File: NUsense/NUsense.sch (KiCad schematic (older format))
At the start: 0 parts

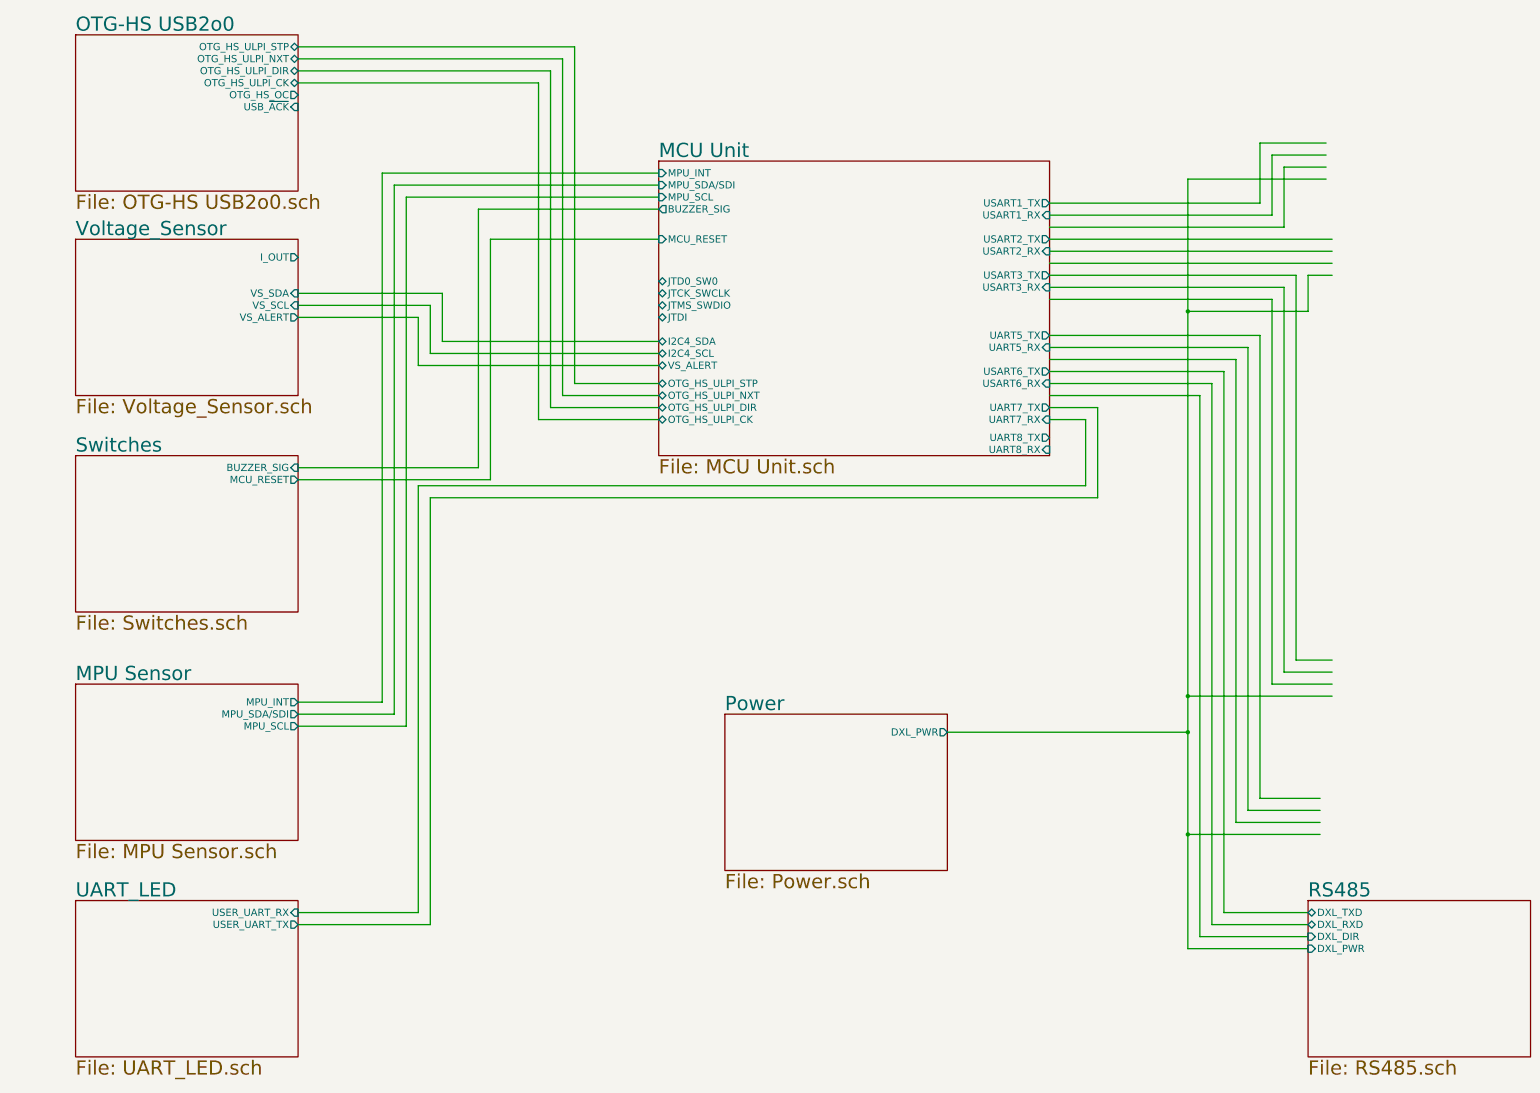
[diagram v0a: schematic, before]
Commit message: Adds all 5 RS485 sheets
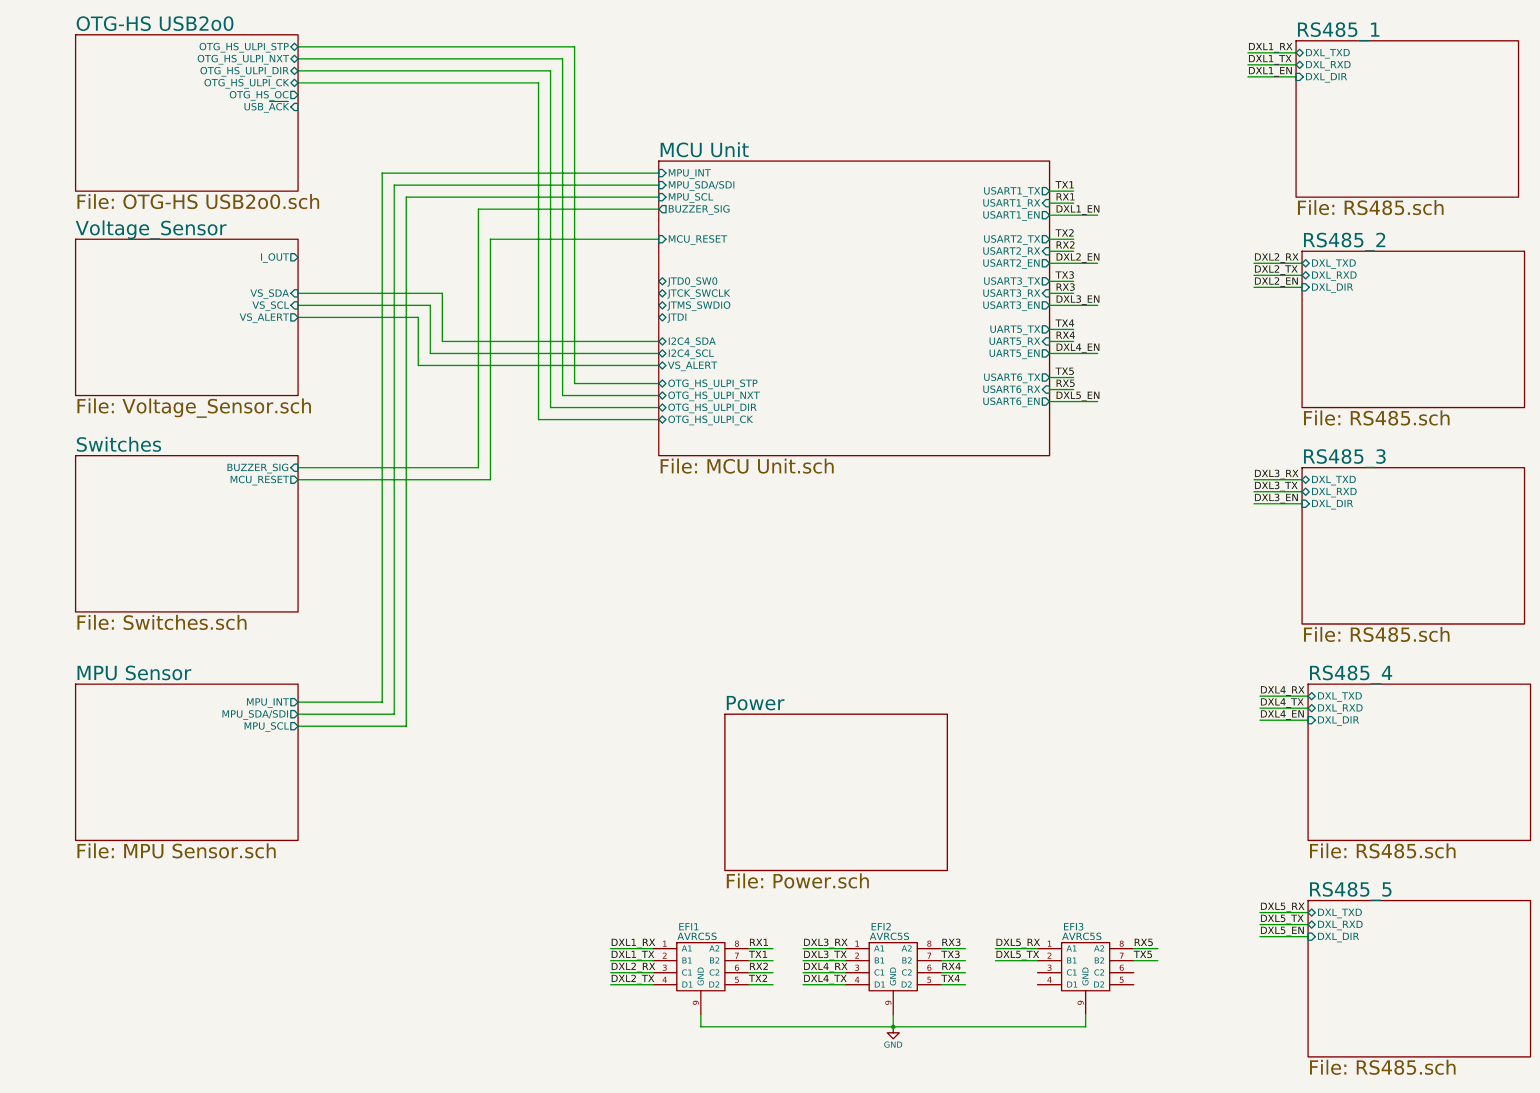
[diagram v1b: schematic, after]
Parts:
- added EFI1, EFI2, EFI3: AVRC5S, Footprints:0805_NET_4, symbol AVRC5S
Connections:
- net labels added: DXL1_EN, DXL1_RX, DXL1_TX, DXL2_EN, DXL2_RX, DXL2_TX, DXL3_EN, DXL3_RX, DXL3_TX, DXL4_EN, DXL4_RX, DXL4_TX, DXL5_EN, DXL5_RX, DXL5_TX, GND, RX1, RX2, RX3, RX4, RX5, TX1, TX2, TX3, TX4, TX5
- wire segments 94 -> 90

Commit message: More Changes
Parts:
- renumbered EFI1 to EFI101, EFI2 to EFI102, EFI3 to EFI103
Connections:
- net labels added: BATT_+, BATT_-, DXL_PWR_EN
- wire segments 90 -> 96
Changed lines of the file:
@@
 F31 "UART5_EN" O R 10450 3800 60
 F32 "USART3_EN" O R 10450 3400 60
+F33 "DXL_PWR_EN" O R 10450 4400 60
 $EndSheet
 $Sheet
@@
 F4 "VS_SDA" I R 4200 3300 60
 F5 "VS_ALERT" O R 4200 3500 60
+F6 "BATT_+" B R 4200 3750 60
+F7 "BATT_-" B R 4200 3850 60
 $EndSheet
 Wire Wire Line
@@
 	4900 2300 7200 2300
 $Comp
-L AVRC5S EFI2
+L AVRC5S EFI102
 U 1 1 5A73E86C
 P 8950 9100
-F 0 "EFI2" H 9050 9630 60  0000 C CNN
+F 0 "EFI102" H 9050 9630 60  0000 C CNN
 F 1 "AVRC5S" H 9120 9550 60  0000 C CNN
 F 2 "Footprints:0805_NET_4" H 9100 9150 60  0001 C CNN
@@
 $EndComp
 $Comp
-L AVRC5S EFI3
+L AVRC5S EFI103
 U 1 1 5A73EA25
 P 10550 9100
-F 0 "EFI3" H 10650 9630 60  0000 C CNN
+F 0 "EFI103" H 10650 9630 60  0000 C CNN
 F 1 "AVRC5S" H 10720 9550 60  0000 C CNN
 F 2 "Footprints:0805_NET_4" H 10700 9150 60  0001 C CNN
@@
 $EndComp
 $Comp
-L AVRC5S EFI1
+L AVRC5S EFI101
 U 1 1 5A73EB9C
 P 7350 9100
-F 0 "EFI1" H 7450 9630 60  0000 C CNN
+F 0 "EFI101" H 7450 9630 60  0000 C CNN
 F 1 "AVRC5S" H 7520 9550 60  0000 C CNN
 F 2 "Footprints:0805_NET_4" H 7500 9150 60  0001 C CNN
@@
 Connection ~ 9150 9400
 $Comp
-L GND #PWR?
+L GND #PWR01
 U 1 1 5A7404A8
 P 9150 9400
-F 0 "#PWR?" H 9150 9150 50  0001 C CNN
+F 0 "#PWR01" H 9150 9150 50  0001 C CNN
 F 1 "GND" H 9150 9250 50  0000 C CNN
 F 2 "" H 9150 9400 50  0001 C CNN
@@
 F0 "Power" 118
 F1 "Power.sch" 118
+F2 "DXL_PWR_EN" I R 9600 6950 60
+F3 "BATT_+" B R 9600 7200 60
+F4 "BATT_-" B R 9600 7300 60
 $EndSheet
 Wire Wire Line
@@
 Wire Wire Line
 	10450 4200 10850 4200
+Wire Wire Line
+	10450 4400 11050 4400
+Text Label 11050 4400 2    60   ~ 0
+DXL_PWR_EN
+Wire Wire Line
+	9600 6950 10300 6950
+Text Label 10300 6950 2    60   ~ 0
+DXL_PWR_EN
+Wire Wire Line
+	4200 3750 4650 3750
+Wire Wire Line
+	4200 3850 4650 3850
+Wire Wire Line
+	9600 7200 10250 7200
+Wire Wire Line
+	9600 7300 10250 7300
+Text Label 10250 7200 2    60   ~ 0
+BATT_+
+Text Label 10250 7300 2    60   ~ 0
+BATT_-
+Text Label 4650 3850 2    60   ~ 0
+BATT_-
+Text Label 4650 3750 2    60   ~ 0
+BATT_+
 $EndSCHEMATC

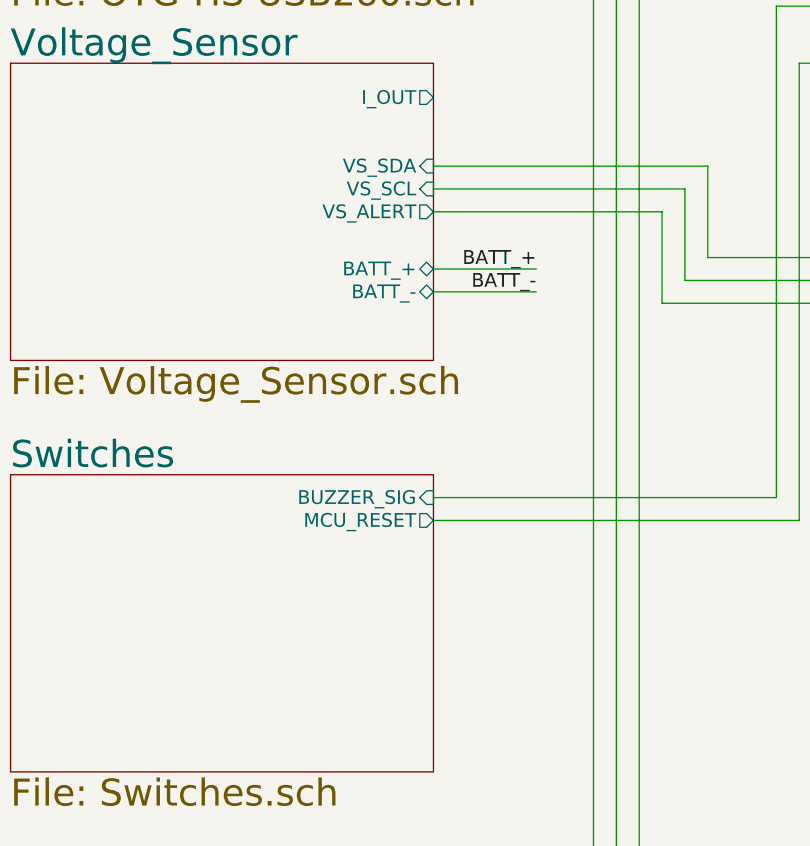
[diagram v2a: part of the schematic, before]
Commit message: Fan PWM
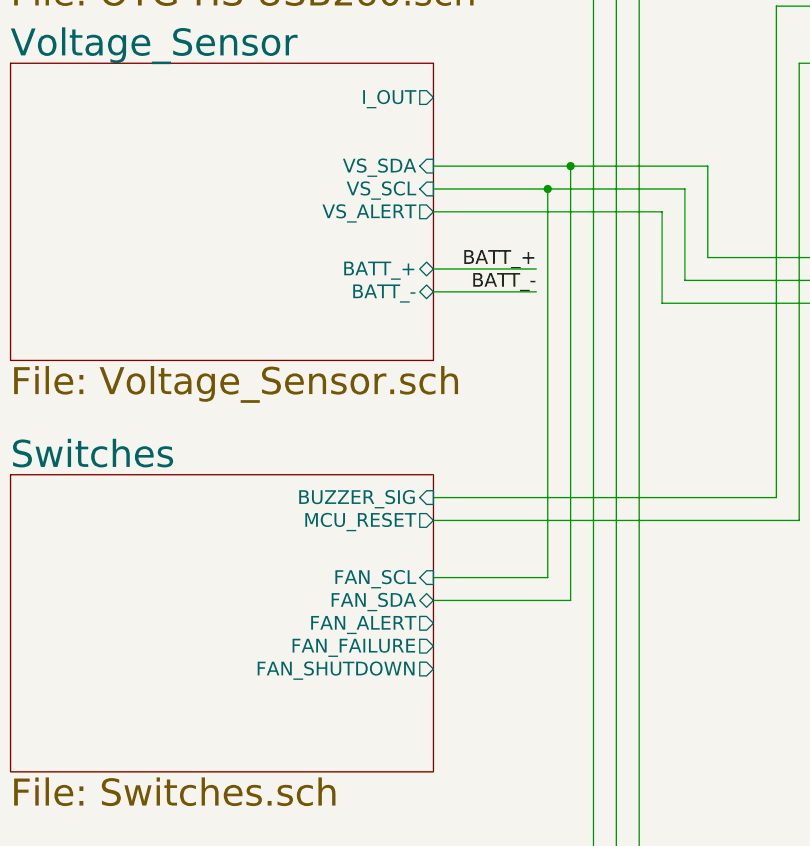
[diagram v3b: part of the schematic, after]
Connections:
- wire segments 96 -> 100
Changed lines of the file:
@@
 F2 "BUZZER_SIG" I R 4200 4750 60
 F3 "MCU_RESET" O R 4200 4850 60
+F4 "FAN_SCL" I R 4200 5100 60
+F5 "FAN_SDA" B R 4200 5200 60
+F6 "FAN_ALERT" O R 4200 5300 60
+F7 "FAN_FAILURE" O R 4200 5400 60
+F8 "FAN_SHUTDOWN" O R 4200 5500 60
 $EndSheet
 $Sheet
@@
 Text Label 4650 3750 2    60   ~ 0
 BATT_+
+Wire Wire Line
+	4800 3300 4800 5200
+Wire Wire Line
+	4800 5200 4200 5200
+Connection ~ 4800 3300
+Wire Wire Line
+	4200 5100 4700 5100
+Wire Wire Line
+	4700 5100 4700 3400
+Connection ~ 4700 3400
 $EndSCHEMATC

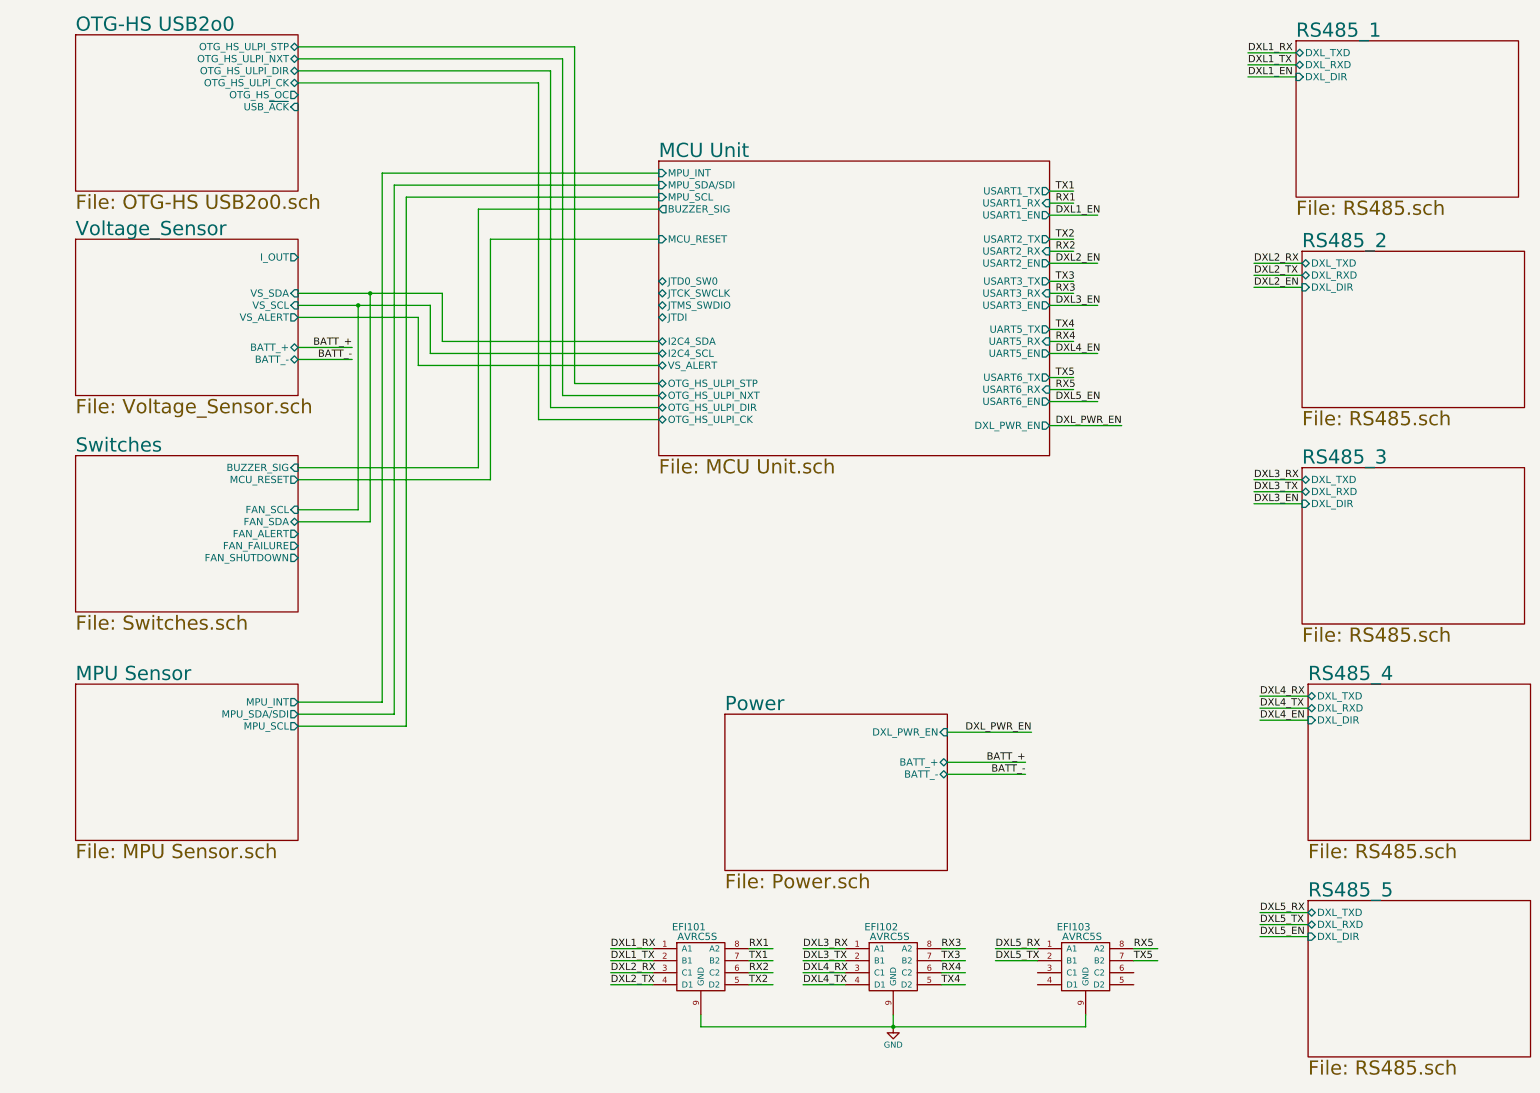
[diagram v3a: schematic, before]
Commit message: Add LED and Button
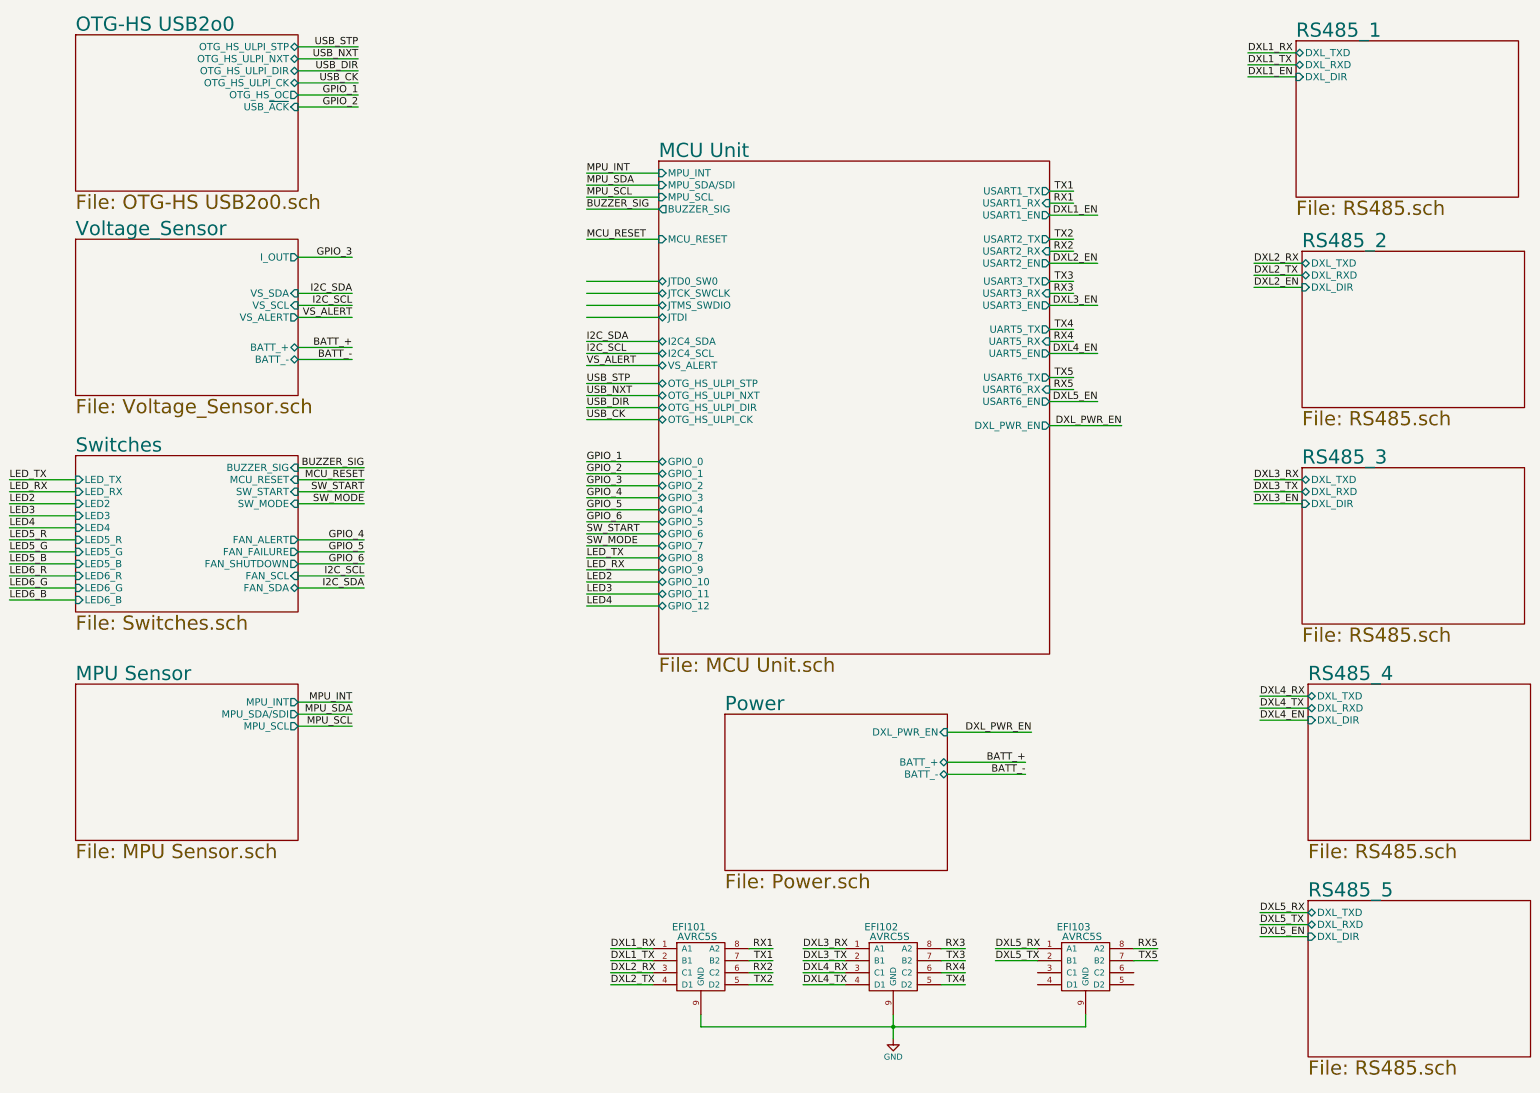
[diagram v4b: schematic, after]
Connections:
- net labels added: BUZZER_SIG, GPIO_1, GPIO_2, GPIO_3, GPIO_4, GPIO_5, GPIO_6, I2C_SCL, I2C_SDA, LED2, LED3, LED4, LED5_B, LED5_G, LED5_R, LED6_B, LED6_G, LED6_R, LED_RX, LED_TX, MCU_RESET, MPU_INT, MPU_SCL, MPU_SDA, SW_MODE, SW_START, USB_CK, USB_DIR, USB_NXT, USB_STP, VS_ALERT
- wire segments 100 -> 122

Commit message: pwm
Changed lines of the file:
@@
 F45 "GPIO_11" B L 7200 5800 60
 F46 "GPIO_12" B L 7200 5900 60
+F47 "TIM1_CH1" O R 10450 4750 60
+F48 "TIM1_CH2" O R 10450 4850 60
+F49 "TIM1_CH3" O R 10450 4950 60
+F50 "TIM8_CH1" O R 10450 5050 60
+F51 "TIM8_CH2" O R 10450 5150 60
+F52 "TIM8_CH3" O R 10450 5250 60
 $EndSheet
 $Sheet
@@
 Text Label 6600 5900 0    60   ~ 0
 LED4
+Wire Wire Line
+	10450 4750 11050 4750
+Wire Wire Line
+	10450 4850 11050 4850
+Wire Wire Line
+	10450 4950 11050 4950
+Wire Wire Line
+	10450 5050 11050 5050
+Wire Wire Line
+	10450 5150 11050 5150
+Wire Wire Line
+	10450 5250 11050 5250
+Text Label 11050 4750 2    60   ~ 0
+LED5_R
+Text Label 11050 4850 2    60   ~ 0
+LED5_G
+Text Label 11050 4950 2    60   ~ 0
+LED5_B
+Text Label 11050 5050 2    60   ~ 0
+LED6_R
+Text Label 11050 5150 2    60   ~ 0
+LED6_G
+Text Label 11050 5250 2    60   ~ 0
+LED6_B
 $EndSCHEMATC

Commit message: Further Cleaning
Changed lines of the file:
@@
 Wire Wire Line
 	4200 1850 4700 1850
-Text Label 4250 1850 0    60   ~ 0
+Text Label 4700 1850 2    60   ~ 0
 USB_DATA
 Wire Wire Line
